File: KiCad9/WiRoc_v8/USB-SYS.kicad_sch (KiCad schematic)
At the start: 20 parts, among them U11 AllwinnerH3, U13 SGM803-RXN3L, Y2 24MHz/18pF

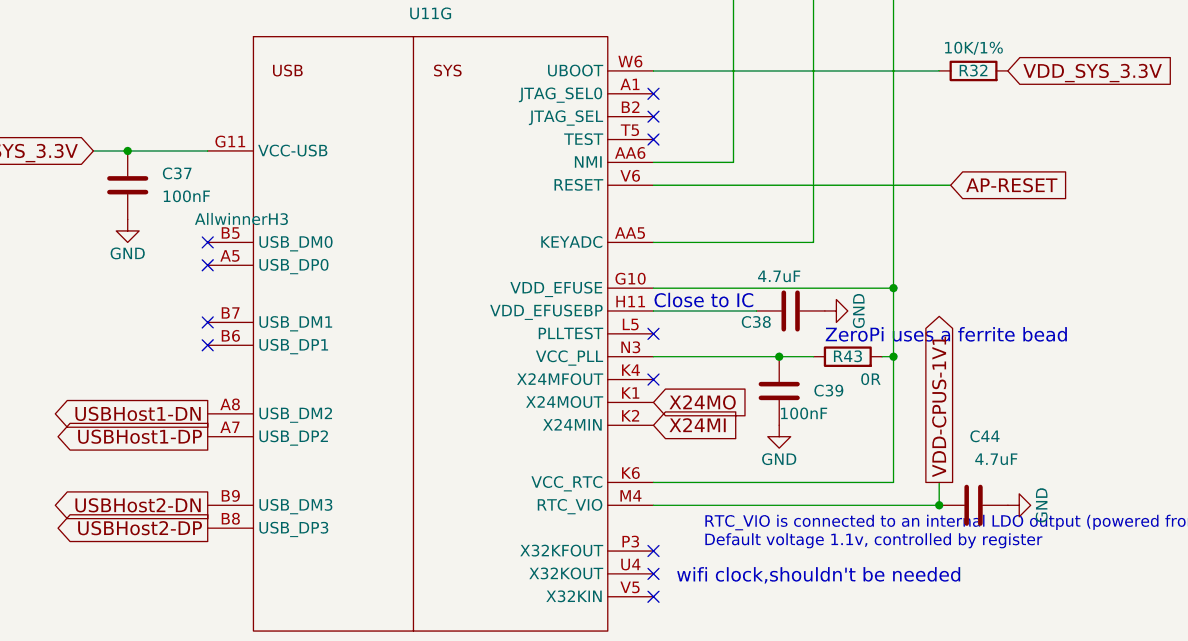
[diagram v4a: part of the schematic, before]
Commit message: change to 10uF in pdn, vdd-dram area to south caps, remove varistor, etc
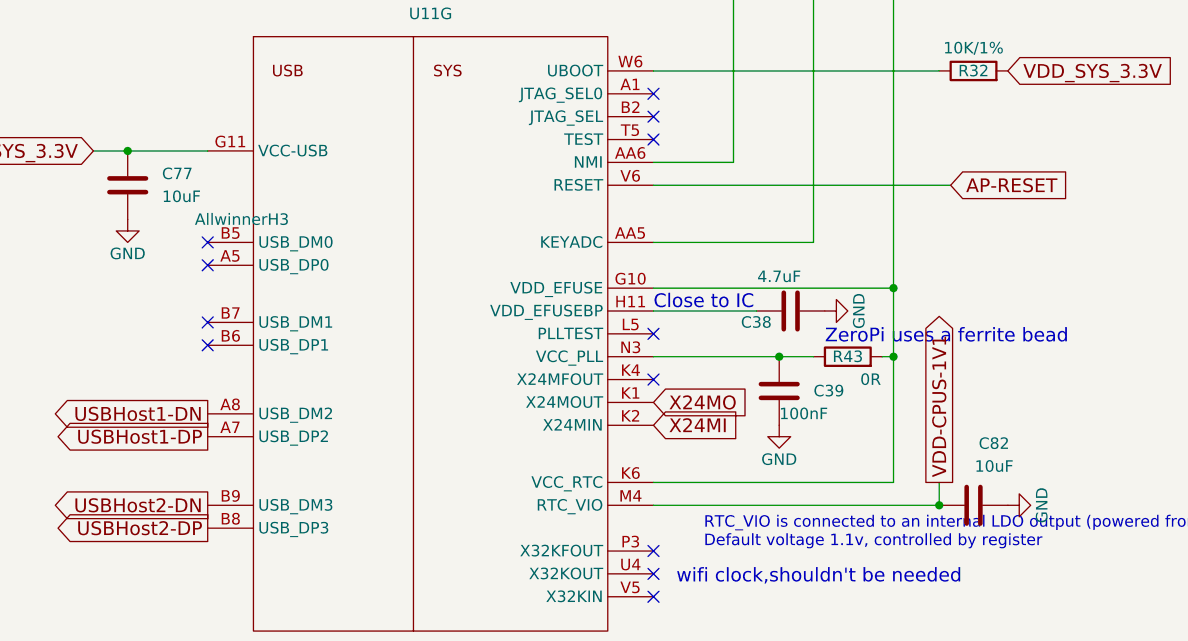
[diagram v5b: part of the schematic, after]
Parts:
- removed C37: 100nF, Capacitor_SMD:C_0402_1005Metric, symbol Device:C
- removed C44: 4.7uF, Capacitor_SMD:C_0402_1005Metric, symbol Device:C
- added C77, C82: 10uF, Capacitor_SMD:C_0402_1005Metric, symbol Device:C
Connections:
- net GND: now also C77.2, C82.2
- net VDD-CPUS-1V1: now also C82.1
- net VDD_SYS_3.3V: now also C77.1
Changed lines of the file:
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@@
 	)
 	(junction
-		(at 36.83 52.07)
-		(diameter 0)
-		(color 0 0 0 0)
-	)
-	(junction
 		(at 87.63 165.1)
 		(diameter 0)
@@
 	)
 	(junction
+		(at 36.83 52.07)
+		(diameter 0)
+		(color 0 0 0 0)
+	)
+	(junction
 		(at 109.22 74.93)
 		(diameter 0)
@@
 	(wire
 		(pts
-			(xy 95.25 55.88) (xy 128.27 55.88)
+			(xy 36.83 52.07) (xy 45.72 52.07)
 		)
 		(stroke
@@
 	(wire
 		(pts
-			(xy 88.9 138.43) (xy 86.36 138.43)
+			(xy 95.25 55.88) (xy 128.27 55.88)
 		)
 		(stroke
@@
 	(wire
 		(pts
-			(xy 85.09 167.64) (xy 87.63 167.64)
+			(xy 88.9 138.43) (xy 86.36 138.43)
 		)
 		(stroke
@@
 	(wire
 		(pts
-			(xy 36.83 52.07) (xy 45.72 52.07)
+			(xy 85.09 167.64) (xy 87.63 167.64)
 		)
 		(stroke
@@
 	(symbol
 		(lib_id "Device:C")
+		(at 36.83 55.88 0)
+		(unit 1)
+		(exclude_from_sim no)
+		(in_bom yes)
+		(on_board yes)
+		(dnp no)
+		(fields_autoplaced yes)
+		(property "Reference" "C77"
+			(at 40.64 54.61 0)
+			(effects
+				(font
+					(size 1.27 1.27)
+				)
+				(justify left)
+			)
+		)
+		(property "Value" "10uF"
+			(at 40.64 57.15 0)
+			(effects
+				(font
+					(size 1.27 1.27)
+				)
+				(justify left)
+			)
+		)
+		(property "Footprint" "Capacitor_SMD:C_0402_1005Metric"
+			(at 37.7952 59.69 0)
+			(effects
+				(font
+					(size 1.27 1.27)
+				)
+				(hide yes)
+			)
+		)
+		(property "Datasheet" "~"
+			(at 36.83 55.88 0)
+			(effects
+				(font
+					(size 1.27 1.27)
+				)
+				(hide yes)
+			)
+		)
+		(property "Description" ""
+			(at 36.83 55.88 0)
+			(effects
+				(font
+					(size 1.27 1.27)
+				)
+				(hide yes)
+			)
+		)
+		(property "LCSC Part #" "C15525"
+			(at 36.83 55.88 0)
+			(effects
+				(font
+					(size 1.27 1.27)
+				)
+				(hide yes)
+			)
+		)
+		(property "Manufacturer" "Samsung Electro-Mechanics"
+			(at 36.83 55.88 0)
+			(effects
+				(font
+					(size 1.27 1.27)
+				)
+				(hide yes)
+			)
+		)
+		(property "ManufacturerPartNumber" "CL05A106MQ5NUNC"
+			(at 36.83 55.88 0)
+			(effects
+				(font
+					(size 1.27 1.27)
+				)
+				(hide yes)
+			)
+		)
+		(property "IncludeInBOM" "TRUE"
+			(at 36.83 55.88 0)
+			(effects
+				(font
+					(size 1.27 1.27)
+				)
+				(hide yes)
+			)
+		)
+		(property "Package" "0402"
+			(at 36.83 55.88 0)
+			(effects
+				(font
+					(size 1.27 1.27)
+				)
+				(hide yes)
+			)
+		)
+		(property "JLCBasicExtended" "Basic"
+			(at 36.83 55.88 0)
+			(effects
+				(font
+					(size 1.27 1.27)
+				)
+				(hide yes)
+			)
+		)
+		(pin "2"
+		)
+		(pin "1"
+		)
+		(instances
+			(project "WiRoc_NanoPi"
+				(path "/8ba0b499-eaca-4cd5-a002-c6bdb610cc8c/eeca7bc5-9dbc-4a35-98ab-67f992cd7f55"
+					(reference "C77")
+					(unit 1)
+				)
+			)
+		)
+	)
+	(symbol
+		(lib_id "Device:C")
 		(at 193.04 55.88 90)
 		(unit 1)
@@
 		(on_board yes)
 		(dnp no)
-		(property "Reference" "C44"
-			(at 132.08 83.82 90)
+		(property "Reference" "C82"
+			(at 133.096 84.582 90)
 			(effects
 				(font
@@
 			)
 		)
-		(property "Value" "4.7uF"
-			(at 133.35 86.36 90)
+		(property "Value" "10uF"
+			(at 133.096 87.122 90)
 			(effects
 				(font
@@
 			)
 		)
-		(property "LCSC Part #" "C23733"
-			(at 130.81 91.44 90)
+		(property "LCSC Part #" "C15525"
+			(at 130.81 91.44 0)
 			(effects
 				(font
@@
 		)
 		(property "Manufacturer" "Samsung Electro-Mechanics"
-			(at 130.81 91.44 90)
+			(at 130.81 91.44 0)
 			(effects
 				(font
@@
 			)
 		)
-		(property "ManufacturerPartNumber" "CL05A475MP5NRNC"
-			(at 130.81 91.44 90)
+		(property "ManufacturerPartNumber" "CL05A106MQ5NUNC"
+			(at 130.81 91.44 0)
 			(effects
 				(font
@@
 		)
 		(property "IncludeInBOM" "TRUE"
-			(at 130.81 91.44 90)
+			(at 130.81 91.44 0)
 			(effects
 				(font
@@
 			)
 		)
-		(property "JLCBasicExtended" "Basic"
-			(at 130.81 91.44 90)
+		(property "Package" "0402"
+			(at 130.81 91.44 0)
 			(effects
 				(font
@@
 			)
 		)
-		(property "Package" "0402"
-			(at 130.81 91.44 90)
+		(property "JLCBasicExtended" "Basic"
+			(at 130.81 91.44 0)
 			(effects
 				(font
@@
 			)
 		)
-		(pin "1"
-		)
 		(pin "2"
 		)
+		(pin "1"
+		)
 		(instances
 			(project "WiRoc_NanoPi"
 				(path "/8ba0b499-eaca-4cd5-a002-c6bdb610cc8c/eeca7bc5-9dbc-4a35-98ab-67f992cd7f55"
-					(reference "C44")
+					(reference "C82")
 					(unit 1)
 				)
@@
 					(unit 1)
 				)
-			)
-		)
-	)
-	(symbol
-		(lib_id "Device:C")
-		(at 36.83 55.88 0)
-		(unit 1)
-		(exclude_from_sim no)
-		(in_bom yes)
-		(on_board yes)
-		(dnp no)
-		(fields_autoplaced yes)
-		(property "Reference" "C37"
-			(at 40.64 54.61 0)
-			(effects
-				(font
-					(size 1.27 1.27)
-				)
-				(justify left)
-			)
-		)
-		(property "Value" "100nF"
-			(at 40.64 57.15 0)
-			(effects
-				(font
-					(size 1.27 1.27)
-				)
-				(justify left)
-			)
-		)
-		(property "Footprint" "Capacitor_SMD:C_0402_1005Metric"
-			(at 37.7952 59.69 0)
-			(effects
-				(font
-					(size 1.27 1.27)
-				)
-				(hide yes)
-			)
-		)
-		(property "Datasheet" "~"
-			(at 36.83 55.88 0)
-			(effects
-				(font
-					(size 1.27 1.27)
-				)
-				(hide yes)
-			)
-		)
-		(property "Description" ""
-			(at 36.83 55.88 0)
-			(effects
-				(font
-					(size 1.27 1.27)
-				)
-				(hide yes)
-			)
-		)
-		(property "IncludeInBOM" "TRUE"
-			(at 36.83 55.88 0)
-			(effects
-				(font
-					(size 1.27 1.27)
-				)
-				(hide yes)
-			)
-		)
-		(property "LCSC Part #" "C1525"
-			(at 36.83 55.88 0)
-			(effects
-				(font
-					(size 1.27 1.27)
-				)
-				(hide yes)
-			)
-		)
-		(property "Manufacturer" "Samsung Electro-Mechanics"
-			(at 36.83 55.88 0)
-			(effects
-				(font
-					(size 1.27 1.27)
-				)
-				(hide yes)
-			)
-		)
-		(property "ManufacturerPartNumber" "CL05B104KO5NNNC"
-			(at 36.83 55.88 0)
-			(effects
-				(font
-					(size 1.27 1.27)
-				)
-				(hide yes)
-			)
-		)
-		(property "JLCBasicExtended" "Basic"
-			(at 36.83 55.88 0)
-			(effects
-				(font
-					(size 1.27 1.27)
-				)
-				(hide yes)
-			)
-		)
-		(property "Package" "0402"
-			(at 36.83 55.88 0)
-			(effects
-				(font
-					(size 1.27 1.27)
-				)
-				(hide yes)
-			)
-		)
-		(pin "2"
-		)
-		(pin "1"
-		)
-		(instances
-			(project "WiRoc_NanoPi"
-				(path "/8ba0b499-eaca-4cd5-a002-c6bdb610cc8c/eeca7bc5-9dbc-4a35-98ab-67f992cd7f55"
-					(reference "C37")
-					(unit 1)
-				)

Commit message: many small changes, change eMMC
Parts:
- C38: value 4.7uF -> 10uF/6.3V; LCSC Part # C23733 -> C15525; ManufacturerPartNumber CL05A475MP5NRNC -> CL05A106MQ5NUNC
- C40, C41: value 18pF -> 22pF; LCSC Part # C1549 -> C1555; ManufacturerPartNumber 0402CG180J500NT -> 0402CG220J500NT
- C77, C82: value 10uF -> 10uF/6.3V
- Y2: value 24MHz/18pF -> 24MHz/CL=12pF
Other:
- note removed: "Note: ZeroPi used 22pF capacitor and crystal has value "XTAL-2520-4P""
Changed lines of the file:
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@@
 		)
 	)
-	(text "Note: ZeroPi used 22pF capacitor and \ncrystal has value \"XTAL-2520-4P\""
-		(exclude_from_sim no)
-		(at 57.15 146.05 0)
-		(effects
-			(font
-				(size 1.524 1.524)
-			)
-			(justify left bottom)
-		)
-	)
 	(text "RTC_VIO is connected to an internal LDO output (powered from VCC_RTC?)\nDefault voltage 1.1v, controlled by register"
 		(exclude_from_sim no)
@@
 			)
 		)
-		(property "Value" "4.7uF"
+		(property "Value" "10uF/6.3V"
 			(at 109.22 66.04 90)
 			(effects
@@
 			)
 		)
-		(property "LCSC Part #" "C23733"
+		(property "LCSC Part #" "C15525"
 			(at 110.49 69.85 90)
 			(effects
@@
 			)
 		)
-		(property "ManufacturerPartNumber" "CL05A475MP5NRNC"
+		(property "ManufacturerPartNumber" "CL05A106MQ5NUNC"
 			(at 110.49 69.85 90)
 			(effects
@@
 			)
 		)
-		(property "Value" "10uF"
+		(property "Value" "10uF/6.3V"
 			(at 40.64 57.15 0)
 			(effects
@@
 			)
 		)
-		(property "Value" "18pF"
+		(property "Value" "22pF"
 			(at 95.25 138.43 0)
 			(effects
@@
 			)
 		)
-		(property "LCSC Part #" "C1549"
+		(property "LCSC Part #" "C1555"
 			(at 92.71 138.43 0)
 			(effects
@@
 			)
 		)
-		(property "ManufacturerPartNumber" "0402CG180J500NT"
+		(property "ManufacturerPartNumber" "0402CG220J500NT"
 			(at 92.71 138.43 0)
 			(effects
@@
 			)
 		)
-		(property "Value" "10uF"
+		(property "Value" "10uF/6.3V"
 			(at 133.096 87.122 90)
 			(effects
@@
 			)
 		)
-		(property "Value" "18pF"
+		(property "Value" "22pF"
 			(at 95.25 121.92 0)
 			(effects
@@
 			)
 		)
-		(property "LCSC Part #" "C1549"
+		(property "LCSC Part #" "C1555"
 			(at 92.71 121.92 0)
 			(effects
@@
 			)
 		)
-		(property "ManufacturerPartNumber" "0402CG180J500NT"
+		(property "ManufacturerPartNumber" "0402CG220J500NT"
 			(at 92.71 121.92 0)
 			(effects
@@
 			)
 		)
-		(property "Value" "24MHz/18pF"
+		(property "Value" "24MHz/CL=12pF"
 			(at 68.58 130.81 0)
 			(effects

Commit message: etc
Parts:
- removed R43: 0R, Resistor_SMD:R_0402_1005Metric, symbol Device:R
- C39: value 100nF -> 10uF/6.3V; LCSC Part # C1525 -> C15525; ManufacturerPartNumber CL05B104KO5NNNC -> CL05A106MQ5NUNC
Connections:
- net VDD_SYS_3.3V: now also C39.2, U11.N3 (VCC_PLL)
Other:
- note removed: "ZeroPi uses a ferrite bead"
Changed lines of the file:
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@@
 	(generator_version "9.0")
 	(paper "A4")
-	(text "ZeroPi uses a ferrite bead"
-		(exclude_from_sim no)
-		(at 114.3 73.66 0)
-		(effects
-			(font
-				(size 1.524 1.524)
-			)
-			(justify left bottom)
-		)
-	)
 	(text "Close to IC"
 		(exclude_from_sim no)
@@
 	(wire
 		(pts
-			(xy 120.65 74.93) (xy 121.92 74.93)
-		)
-		(stroke
-			(width 0)
-			(type default)
-		)
-	)
-	(wire
-		(pts
 			(xy 127 91.44) (xy 127 88.9)
 		)
@@
 	(wire
 		(pts
-			(xy 109.22 74.93) (xy 113.03 74.93)
+			(xy 109.22 74.93) (xy 121.92 74.93)
 		)
 		(stroke
@@
 	(symbol
 		(lib_id "Device:R")
-		(at 116.84 74.93 90)
-		(unit 1)
-		(exclude_from_sim no)
-		(in_bom yes)
-		(on_board yes)
-		(dnp no)
-		(property "Reference" "R43"
-			(at 116.84 74.93 90)
-			(effects
-				(font
-					(size 1.27 1.27)
-				)
-			)
-		)
-		(property "Value" "0R"
-			(at 119.38 77.47 90)
-			(effects
-				(font
-					(size 1.27 1.27)
-				)
-			)
-		)
-		(property "Footprint" "Resistor_SMD:R_0402_1005Metric"
-			(at 116.84 76.708 90)
-			(effects
-				(font
-					(size 1.27 1.27)
-				)
-				(hide yes)
-			)
-		)
-		(property "Datasheet" "~"
-			(at 116.84 74.93 0)
-			(effects
-				(font
-					(size 1.27 1.27)
-				)
-				(hide yes)
-			)
-		)
-		(property "Description" ""
-			(at 116.84 74.93 0)
-			(effects
-				(font
-					(size 1.27 1.27)
-				)
-				(hide yes)
-			)
-		)
-		(property "JLCBasicExtended" "Basic"
-			(at 116.84 74.93 90)
-			(effects
-				(font
-					(size 1.27 1.27)
-				)
-				(hide yes)
-			)
-		)
-		(property "IncludeInBOM" "TRUE"
-			(at 116.84 74.93 90)
-			(effects
-				(font
-					(size 1.27 1.27)
-				)
-				(hide yes)
-			)
-		)
-		(property "LCSC Part #" "C17168"
-			(at 116.84 74.93 90)
-			(effects
-				(font
-					(size 1.27 1.27)
-				)
-				(hide yes)
-			)
-		)
-		(property "Manufacturer" "Uniroyal Elec"
-			(at 116.84 74.93 90)
-			(effects
-				(font
-					(size 1.27 1.27)
-				)
-				(hide yes)
-			)
-		)
-		(property "ManufacturerPartNumber" "0402WGF0000TCE"
-			(at 116.84 74.93 90)
-			(effects
-				(font
-					(size 1.27 1.27)
-				)
-				(hide yes)
-			)
-		)
-		(property "Package" "0402"
-			(at 116.84 74.93 90)
-			(effects
-				(font
-					(size 1.27 1.27)
-				)
-				(hide yes)
-			)
-		)
-		(pin "2"
-		)
-		(pin "1"
-		)
-		(instances
-			(project "WiRoc_NanoPi"
-				(path "/8ba0b499-eaca-4cd5-a002-c6bdb610cc8c/eeca7bc5-9dbc-4a35-98ab-67f992cd7f55"
-					(reference "R43")
-					(unit 1)
-				)
-			)
-		)
-	)
-	(symbol
-		(lib_id "Device:R")
 		(at 81.28 167.64 90)
 		(unit 1)
@@
 			)
 		)
-		(property "Value" "100nF"
+		(property "Value" "10uF/6.3V"
 			(at 109.22 81.28 0)
 			(effects
@@
 			)
 		)
-		(property "LCSC Part #" "C1525"
+		(property "LCSC Part #" "C15525"
 			(at 109.22 78.74 0)
 			(effects
@@
 			)
 		)
-		(property "ManufacturerPartNumber" "CL05B104KO5NNNC"
+		(property "ManufacturerPartNumber" "CL05A106MQ5NUNC"
 			(at 109.22 78.74 0)
 			(effects

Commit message: add ethernet etc
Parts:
- added R19: 6K/1%, symbol Device:R
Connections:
- net GND: now also R19.1
- net EPHY_TXN: now reaches U11.A3 (EPHY_TXN)
- net EPHY_RXN: now reaches U11.A4 (EPHY_RXN)
- net EPHY_TXP: now reaches U11.B3 (EPHY_TXP)
- net EPHY_RXP: now reaches U11.B4 (EPHY_RXP)
- net at U11.F6 (EPHY_RTX): now also R19.2
- net LORARS renamed LORAIRQ
- no-connect marks 48 -> 43
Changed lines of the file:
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@@
 		)
 	)
+	(text "Close to IC"
+		(exclude_from_sim no)
+		(at 177.8 107.95 0)
+		(effects
+			(font
+				(size 1.524 1.524)
+			)
+		)
+	)
 	(text "RTC_VIO is connected to an internal LDO output (powered from VCC_RTC?)\nDefault voltage 1.1v, controlled by register"
 		(exclude_from_sim no)
@@
 	)
 	(no_connect
-		(at 196.85 97.79)
-	)
-	(no_connect
 		(at 245.11 88.9)
 	)
@@
 	)
 	(no_connect
-		(at 196.85 105.41)
-	)
-	(no_connect
 		(at 95.25 45.72)
 	)
@@
 	)
 	(no_connect
-		(at 196.85 102.87)
-	)
-	(no_connect
-		(at 196.85 95.25)
-	)
-	(no_connect
 		(at 72.39 160.02)
 	)
@@
 	)
 	(no_connect
-		(at 196.85 100.33)
-	)
-	(no_connect
 		(at 95.25 96.52)
 	)
@@
 	(wire
 		(pts
+			(xy 180.34 105.41) (xy 196.85 105.41)
+		)
+		(stroke
+			(width 0)
+			(type default)
+		)
+	)
+	(wire
+		(pts
 			(xy 125.73 130.81) (xy 125.73 134.62)
 		)
@@
 		)
 	)
+	(global_label "EPHY_TXN"
+		(shape output)
+		(at 196.85 102.87 180)
+		(fields_autoplaced yes)
+		(effects
+			(font
+				(size 1.524 1.524)
+			)
+			(justify right)
+		)
+		(property "Intersheetrefs" "${INTERSHEET_REFS}"
+			(at 182.8772 102.87 0)
+			(effects
+				(font
+					(size 1.27 1.27)
+				)
+				(justify right)
+				(hide yes)
+			)
+		)
+	)
 	(global_label "VDD_SYS_3.3V"
 		(shape input)
@@
 		)
 	)
-	(global_label "LORARS"
+	(global_label "EPHY_TXP"
 		(shape output)
+		(at 196.85 100.33 180)
+		(fields_autoplaced yes)
+		(effects
+			(font
+				(size 1.524 1.524)
+			)
+			(justify right)
+		)
+		(property "Intersheetrefs" "${INTERSHEET_REFS}"
+			(at 182.9498 100.33 0)
+			(effects
+				(font
+					(size 1.27 1.27)
+				)
+				(justify right)
+				(hide yes)
+			)
+		)
+	)
+	(global_label "EPHY_RXN"
+		(shape input)
+		(at 196.85 97.79 180)
+		(fields_autoplaced yes)
+		(effects
+			(font
+				(size 1.524 1.524)
+			)
+			(justify right)
+		)
+		(property "Intersheetrefs" "${INTERSHEET_REFS}"
+			(at 182.5143 97.79 0)
+			(effects
+				(font
+					(size 1.27 1.27)
+				)
+				(justify right)
+				(hide yes)
+			)
+		)
+	)
+	(global_label "LORAIRQ"
+		(shape input)
 		(at 72.39 185.42 0)
 		(fields_autoplaced yes)
@@
 		)
 		(property "Intersheetrefs" "${INTERSHEET_REFS}"
-			(at 83.7274 185.42 0)
+			(at 84.6937 185.42 0)
 			(effects
 				(font
@@
 		)
 	)
+	(global_label "EPHY_RXP"
+		(shape input)
+		(at 196.85 95.25 180)
+		(fields_autoplaced yes)
+		(effects
+			(font
+				(size 1.524 1.524)
+			)
+			(justify right)
+		)
+		(property "Intersheetrefs" "${INTERSHEET_REFS}"
+			(at 182.5869 95.25 0)
+			(effects
+				(font
+					(size 1.27 1.27)
+				)
+				(justify right)
+				(hide yes)
+			)
+		)
+	)
 	(global_label "VDD1V1-EPHY"
 		(shape input)
@@
 	)
 	(symbol
+		(lib_id "power:GND")
+		(at 172.72 105.41 270)
+		(unit 1)
+		(exclude_from_sim no)
+		(in_bom yes)
+		(on_board yes)
+		(dnp no)
+		(property "Reference" "#PWR014"
+			(at 166.37 105.41 0)
+			(effects
+				(font
+					(size 1.27 1.27)
+				)
+				(hide yes)
+			)
+		)
+		(property "Value" "GND"
+			(at 168.91 105.41 0)
+			(effects
+				(font
+					(size 1.27 1.27)
+				)
+			)
+		)
+		(property "Footprint" ""
+			(at 172.72 105.41 0)
+			(effects
+				(font
+					(size 1.27 1.27)
+				)
+				(hide yes)
+			)
+		)
+		(property "Datasheet" ""
+			(at 172.72 105.41 0)
+			(effects
+				(font
+					(size 1.27 1.27)
+				)
+				(hide yes)
+			)
+		)
+		(property "Description" ""
+			(at 172.72 105.41 0)
+			(effects
+				(font
+					(size 1.27 1.27)
+				)
+				(hide yes)
+			)
+		)
+		(pin "1"
+		)
+		(instances
+			(project "WiRoc_NanoPi"
+				(path "/8ba0b499-eaca-4cd5-a002-c6bdb610cc8c/eeca7bc5-9dbc-4a35-98ab-67f992cd7f55"
+					(reference "#PWR014")
+					(unit 1)
+				)
+			)
+		)
+	)
+	(symbol
 		(lib_id "Device:R")
 		(at 81.28 167.64 90)
@@
 					(unit 1)
 				)
+			)
+		)
+	)
+	(symbol
+		(lib_id "Device:R")
+		(at 176.53 105.41 90)
+		(unit 1)
+		(exclude_from_sim no)
+		(in_bom yes)
+		(on_board yes)
+		(dnp no)
+		(fields_autoplaced yes)
+		(property "Reference" "R19"
+			(at 176.53 99.06 90)
+			(effects
+				(font
+					(size 1.27 1.27)
+				)
+			)
+		)
+		(property "Value" "6K/1%"
+			(at 176.53 101.6 90)
+			(effects
+				(font
+					(size 1.27 1.27)
+				)
+			)
+		)
+		(property "Footprint" ""
+			(at 176.53 107.188 90)
+			(effects
+				(font
+					(size 1.27 1.27)
+				)
+				(hide yes)
+			)
+		)
+		(property "Datasheet" "~"
+			(at 176.53 105.41 0)
+			(effects
+				(font
+					(size 1.27 1.27)
+				)
+				(hide yes)
+			)
+		)
+		(property "Description" "Resistor"
+			(at 176.53 105.41 0)
+			(effects
+				(font
+					(size 1.27 1.27)
+				)
+				(hide yes)
+			)
+		)
+		(pin "2"
+		)
+		(pin "1"
+		)
+		(instances
+			(project ""
+				(path "/8ba0b499-eaca-4cd5-a002-c6bdb610cc8c/eeca7bc5-9dbc-4a35-98ab-67f992cd7f55"
+					(reference "R19")
+					(unit 1)
+				)
